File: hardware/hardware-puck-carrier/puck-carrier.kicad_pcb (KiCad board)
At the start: 4 copper layers, 46 x 46 mm, 124 parts, among them J1 LiPo 400-500mAh protected, Q1 AO3400A, Q2 AO3400A, Q3 AO3400A, Q4 AO3400A, Q5 AO3400A, U1 MDBT50Q-1MV2, U10 XC6206P182MR 1.8V->AS7341 only, U11 USBLC6-2SC6, U2 TPS61023, U3 AS7341, U4 FDC1004, U5 MS5837-02BA, U6 DS18B20U+, U7 MCP73832T-2ACI/OT, U8 LSM6DSO, U9 IM69D130

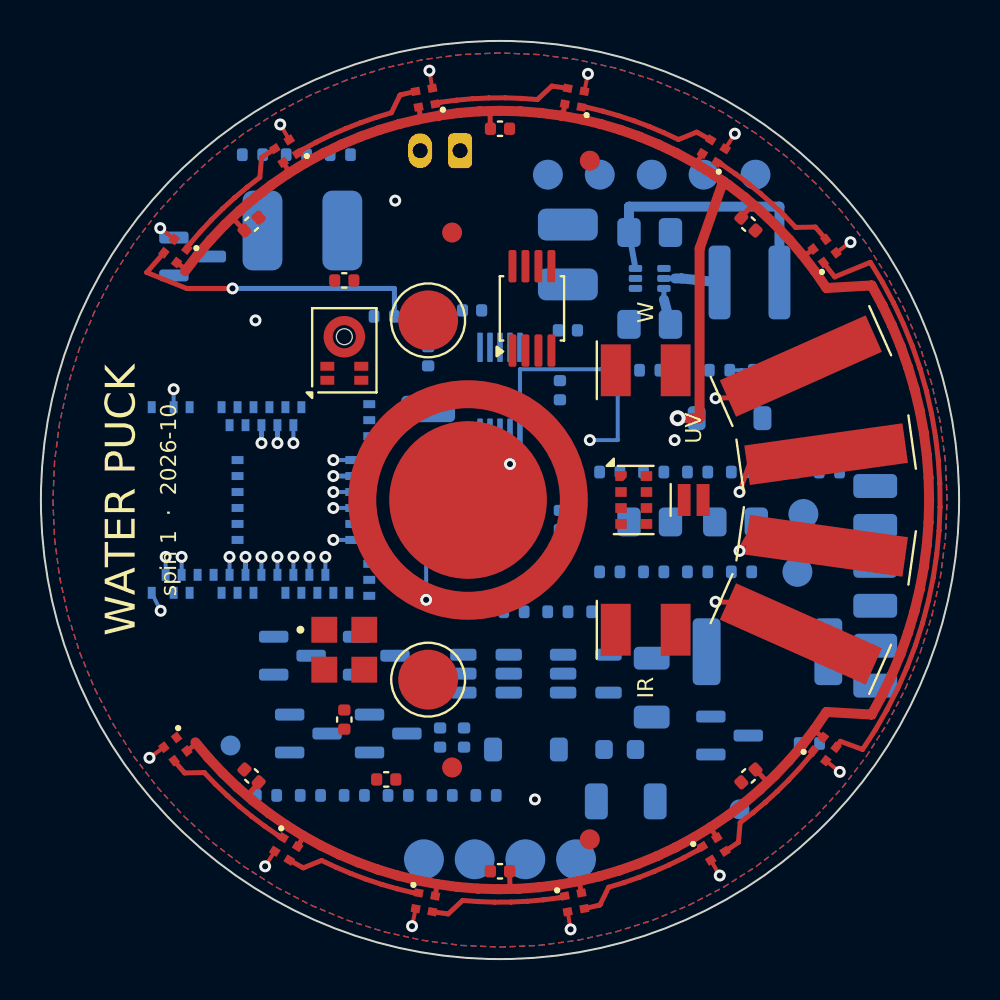
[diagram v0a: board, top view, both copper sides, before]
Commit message: Routing pass: 130 -> 19 signal opens, 0 DRC errors
Scripted 3V3 fan-out, hand routes under the FDC pads, Freerouting rounds on
a filtered router view (scripts/router). GND/3V3 pours now fragmented (21/9
islands); 19 signal connections still open, listed in the changelog.

Co-Authored-By: Claude Fable 5.1 <noreply@anthropic.com>
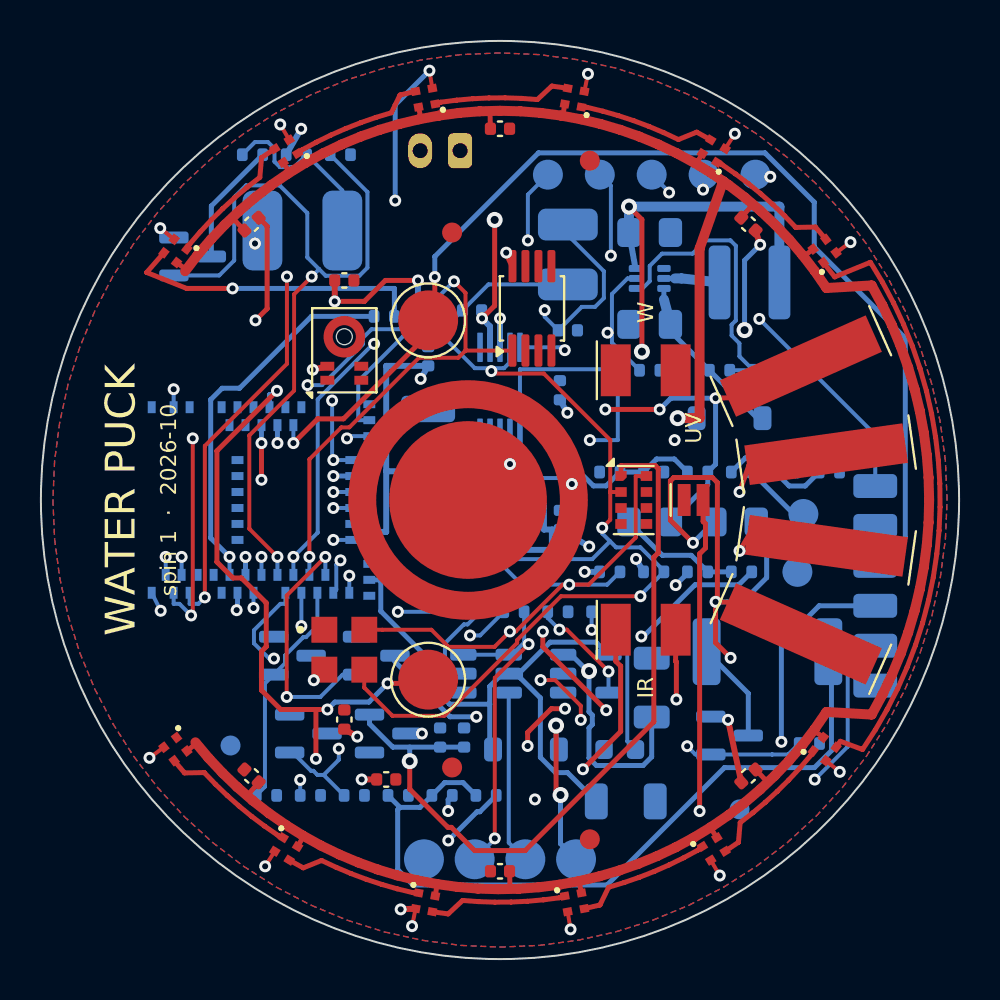
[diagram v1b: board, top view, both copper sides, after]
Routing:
- net GND: track 12.7 -> 139.4 mm, vias 18 -> 25
- net 3V3: track 0.00 -> 81.5 mm, vias 0 -> 17
- net EXP_A5: track 0.00 -> 69.0 mm, vias 0 -> 5
- net SDA: track 0.90 -> 67.0 mm, vias 1 -> 5
- net EC_B: track 1.61 -> 64.5 mm, vias 2 -> 7
- net EXP_A4: track 0.90 -> 56.9 mm, vias 1 -> 2
- net SCL: track 0.00 -> 55.8 mm, vias 0 -> 3
- net EXP_00: track 0.00 -> 48.7 mm, vias 0 -> 4
- net VBAT: track 14.5 -> 60.9 mm, vias 0 -> 3
- net 5V: track 1.84 -> 47.1 mm
- net BTN_DFU: track 0.90 -> 45.8 mm, vias 1 -> 2
- net SWCLK: track 0.00 -> 40.2 mm, vias 0 -> 3
- net PIEZO: track 0.90 -> 40.5 mm, vias 1 -> 2
- net 1V8: track 0.00 -> 39.2 mm, vias 0 -> 1
- net HEATER_EN: track 0.00 -> 37.6 mm, vias 0 -> 2
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
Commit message: Routing: 49 -> 28 unconnected, grid router tools, Codex evening pass logged
Move the module 3V3 trunk off the east pad column, route EC_A and EC_BIAS,
bridge the 3V3 plane pieces, stitch 16 GND islands. 0 DRC errors, parity 0.
Add geom_export/grid_router/apply_plans/gnd_stitch/plot_region and the
strip/riploop/pin_swap helpers; record every strategy that plateaued.

Co-Authored-By: Claude Fable 5.1 <noreply@anthropic.com>
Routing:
- net 3V3: track 81.5 -> 134.4 mm, vias 17 -> 23
- net GND: track 139.4 -> 152.5 mm, vias 25 -> 38
- net EC_A: track 36.9 -> 44.8 mm, vias 4 -> 6
- net EC_BIAS: track 13.3 -> 16.1 mm, vias 0 -> 2
- net EC_SENSE_B: track 1.83 -> 4.32 mm, vias 2 -> 3
- net EC_SENSE_A: vias 1 -> 2
